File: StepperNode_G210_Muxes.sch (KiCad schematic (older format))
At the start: 6 parts

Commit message: Updated node core connector pages and added interlocks.
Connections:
- net labels removed: CHA_STEP_DIR
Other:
- note added: "Direction High = B-Y"
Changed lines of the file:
@@
 	7150 3700 7950 3700
-Wire Wire Line
-	7150 3800 7950 3800
 Wire Wire Line
 	7150 3900 7950 3900
@@
 	0    1    1    0
 $EndComp
-Text Label 7200 3500 0    60   ~ 0
-CHA_STEP2_STEP
-Text Label 7200 3600 0    60   ~ 0
-CHB_STEP2_STEP
 Text Label 7200 3700 0    60   ~ 0
 STEP2_STEP
-Text Label 7200 3800 0    60   ~ 0
-CHA_STEP2_DIR
-Text Label 7200 3900 0    60   ~ 0
-CHB_STEP2_DIR
 Text Label 7200 4000 0    60   ~ 0
 STEP2_DIR
-Text Label 5350 3500 0    60   ~ 0
-CHB_STEP1_DIR
 Text Label 5350 3600 0    60   ~ 0
 STEP1_DIR
-Text Label 5350 3700 0    60   ~ 0
-CHA_STEP1_STEP
-Text Label 5350 3800 0    60   ~ 0
-CHB_STEP1_STEP
 Text Label 5350 3900 0    60   ~ 0
 STEP1_STEP
@@
 	0    1    1    0
 $EndComp
-Text Label 7200 5300 0    60   ~ 0
-CHA_STEP4_STEP
-Text Label 7200 5400 0    60   ~ 0
-CHB_STEP4_STEP
-Text Label 7200 5500 0    60   ~ 0
-STEP4_STEP
-Text Label 7200 5600 0    60   ~ 0
-CHA_STEP4_DIR
-Text Label 7200 5700 0    60   ~ 0
-CHB_STEP4_DIR
 Text Label 7200 5800 0    60   ~ 0
 STEP4_DIR
-Text Label 5350 5200 0    60   ~ 0
-CHA_STEP3_DIR
-Text Label 5350 5300 0    60   ~ 0
-CHB_STEP3_DIR
 Text Label 5350 5400 0    60   ~ 0
 STEP3_DIR
-Text Label 5350 5500 0    60   ~ 0
-CHA_STEP3_STEP
-Text Label 5350 5600 0    60   ~ 0
-CHB_STEP3_STEP
 Text Label 5350 5700 0    60   ~ 0
 STEP3_STEP
@@
 	0    1    1    0
 $EndComp
-Text Label 7000 7550 0    60   ~ 0
-CHA_STEP6_STEP
-Text Label 7000 7650 0    60   ~ 0
-CHB_STEP6_STEP
 Text Label 7000 7750 0    60   ~ 0
 STEP6_STEP
-Text Label 7000 7850 0    60   ~ 0
-CHA_STEP6_DIR
-Text Label 7000 7950 0    60   ~ 0
-CHB_STEP6_DIR
 Text Label 7000 8050 0    60   ~ 0
 STEP6_DIR
-Text Label 5150 7450 0    60   ~ 0
-CHA_STEP5_DIR
-Text Label 5150 7550 0    60   ~ 0
-CHB_STEP5_DIR
 Text Label 5150 7650 0    60   ~ 0
 STEP5_DIR
-Text Label 5150 7750 0    60   ~ 0
-CHA_STEP5_STEP
-Text Label 5150 7850 0    60   ~ 0
-CHB_STEP5_STEP
 Text Label 5150 7950 0    60   ~ 0
 STEP5_STEP
@@
 Text HLabel 5150 3300 0    60   Input ~ 0
 STEP_DIR_CTRL
+Text HLabel 5150 3500 0    60   Input ~ 0
+CHA_STEP1_DIR
+Text HLabel 5150 3800 0    60   Input ~ 0
+CHA_STEP1_STEP
+Text HLabel 7950 3800 2    60   Input ~ 0
+CHB_STEP2_DIR
+Text HLabel 7950 3600 2    60   Input ~ 0
+CHA_STEP2_STEP
 Text HLabel 5150 3400 0    60   Input ~ 0
-CHA_STEP1_DIR
+CHB_STEP1_DIR
 Text HLabel 5150 3700 0    60   Input ~ 0
-CHA_STEP1_STEP
+CHB_STEP1_STEP
 Text HLabel 7950 3900 2    60   Input ~ 0
-CHB_STEP2_DIR
+CHA_STEP2_DIR
 Text HLabel 7950 3500 2    60   Input ~ 0
-CHA_STEP2_STEP
-Text Label 5350 3400 0    60   ~ 0
-CHA_STEP_DIR
-Text HLabel 5150 3500 0    60   Input ~ 0
-CHB_STEP1_DIR
-Text HLabel 5150 3800 0    60   Input ~ 0
-CHB_STEP1_STEP
-Text HLabel 7950 3800 2    60   Input ~ 0
-CHA_STEP2_DIR
-Text HLabel 7950 3600 2    60   Input ~ 0
 CHB_STEP2_STEP
+Text HLabel 5150 5300 0    60   Input ~ 0
+CHA_STEP3_DIR
+Text HLabel 5150 5600 0    60   Input ~ 0
+CHA_STEP3_STEP
 Text HLabel 5150 5200 0    60   Input ~ 0
-CHA_STEP3_DIR
+CHB_STEP3_DIR
 Text HLabel 5150 5500 0    60   Input ~ 0
-CHA_STEP3_STEP
-Text HLabel 5150 5300 0    60   Input ~ 0
-CHB_STEP3_DIR
-Text HLabel 5150 5600 0    60   Input ~ 0
 CHB_STEP3_STEP
+Text HLabel 7950 5600 2    60   Input ~ 0
+CHB_STEP4_DIR
+Text HLabel 7950 5400 2    60   Input ~ 0
+CHA_STEP4_STEP
 Text HLabel 7950 5700 2    60   Input ~ 0
-CHB_STEP4_DIR
+CHA_STEP4_DIR
 Text HLabel 7950 5300 2    60   Input ~ 0
-CHA_STEP4_STEP
-Text HLabel 7950 5600 2    60   Input ~ 0
-CHA_STEP4_DIR
-Text HLabel 7950 5400 2    60   Input ~ 0
 CHB_STEP4_STEP
+Text HLabel 4950 7550 0    60   Input ~ 0
+CHA_STEP5_DIR
+Text HLabel 4950 7850 0    60   Input ~ 0
+CHA_STEP5_STEP
 Text HLabel 4950 7450 0    60   Input ~ 0
-CHA_STEP5_DIR
+CHB_STEP5_DIR
 Text HLabel 4950 7750 0    60   Input ~ 0
-CHA_STEP5_STEP
-Text HLabel 4950 7550 0    60   Input ~ 0
-CHB_STEP5_DIR
-Text HLabel 4950 7850 0    60   Input ~ 0
 CHB_STEP5_STEP
+Text HLabel 7750 7850 2    60   Input ~ 0
+CHB_STEP6_DIR
+Text HLabel 7750 7650 2    60   Input ~ 0
+CHA_STEP6_STEP
 Text HLabel 7750 7950 2    60   Input ~ 0
-CHB_STEP6_DIR
+CHA_STEP6_DIR
 Text HLabel 7750 7550 2    60   Input ~ 0
-CHA_STEP6_STEP
-Text HLabel 7750 7850 2    60   Input ~ 0
-CHA_STEP6_DIR
-Text HLabel 7750 7650 2    60   Input ~ 0
 CHB_STEP6_STEP
+Text Notes 4350 2650 0    60   ~ 0
+Direction High = B-Y
+Wire Wire Line
+	7150 3800 7950 3800
+Text Label 7200 5500 0    60   ~ 0
+STEP4_STEP
 $EndSCHEMATC

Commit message: Remove Gimbal Functions
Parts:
- removed P? (x2): CONN_01X08_2MNT, symbol CONN_01X08_2MNT
- removed U? (x3): 74HCT157, symbol 74HCT157
- added C?: C_100nF_50V, RLOOP_FOOTPRINTS:rLoop_C_0603, symbol C_100nF_50V
- added U?: SN74HCT157D, RLOOP_FOOTPRINTS:rLoop_SOIC_16, symbol SN74HCT157D
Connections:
- net labels added: BRAKE1_DIR, BRAKE1_STEP, BRAKE2_DIR, BRAKE2_STEP, CHA_BRAKE1_DIR, CHA_BRAKE1_STEP, CHA_BRAKE2_DIR, CHA_BRAKE2_STEP, CHB_BRAKE1_DIR, CHB_BRAKE1_STEP, CHB_BRAKE2_DIR, CHB_BRAKE2_STEP
- net labels removed: CHA_STEP1_DIR, CHA_STEP1_STEP, CHA_STEP2_DIR, CHA_STEP2_STEP, CHA_STEP3_DIR, CHA_STEP3_STEP, CHA_STEP4_DIR, CHA_STEP4_STEP, CHA_STEP5_DIR, CHA_STEP5_STEP, CHA_STEP6_DIR, CHA_STEP6_STEP, CHB_STEP1_DIR, CHB_STEP1_STEP, CHB_STEP2_DIR, CHB_STEP2_STEP, CHB_STEP3_DIR, CHB_STEP3_STEP, CHB_STEP4_DIR, CHB_STEP4_STEP, CHB_STEP5_DIR, CHB_STEP5_STEP, CHB_STEP6_DIR, CHB_STEP6_STEP, STEP1_DIR, STEP1_STEP, STEP2_DIR, STEP2_STEP, STEP3_DIR, STEP3_STEP, STEP4_DIR, STEP4_STEP, STEP5_DIR, STEP5_STEP, STEP6_DIR, STEP6_STEP
- wire segments 60 -> 20
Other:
- note added: "Left and Right Brake Controllers"
- note removed: "15TTL load output capacity"
- note removed: "Fwd Left and Aft Left Gimbal Controller"
- note removed: "Fwd Right and Aft Right Gimbal Controller"
- note removed: "Left and Right brake controller."
- note removed: "Step 1 and 2, Left and Right brake drive controllers."
- note removed: "Step 3 and 4, Fwd Left and Aft Left Gimbal"
- note removed: "Step 5 and 6, Fwd Right and Aft Right Gimbal"

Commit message: First Revision -
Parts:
- removed P?: CONN_01X08_2MNT, symbol CONN_01X08_2MNT
- added P1: TE_640456-8, RLOOP_FOOTPRINTS:rLoop_TE640456-8, symbol TE_640456-8
- gave numbers to parts that had none: 2
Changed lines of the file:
@@
 Text Notes 5000 3500 0    60   ~ 0
 At 5V, VinH = 2V\nSafe to interface with 3.3V
-$Comp
-L CONN_01X08_2MNT P?
-U 1 1 575000E8
-P 12700 4300
-F 0 "P?" H 12700 4750 50  0000 C CNN
-F 1 "CONN_01X08_2MNT" V 12800 4300 50  0000 C CNN
-F 2 "" H 12700 4300 50  0000 C CNN
-F 3 "" H 12700 4300 50  0000 C CNN
-	1    12700 4300
-	1    0    0    -1
-$EndComp
 Text Notes 12150 4950 0    60   ~ 0
 Left and Right Brake Controllers
@@
 	12500 4350 11650 4350
 $Comp
-L GNDD #PWR?
+L GNDD #PWR6
 U 1 1 575000F3
 P 12500 4150
-F 0 "#PWR?" H 12500 3900 50  0001 C CNN
+F 0 "#PWR6" H 12500 3900 50  0001 C CNN
 F 1 "GNDD" H 12500 4000 50  0000 C CNN
 F 2 "" H 12500 4150 50  0000 C CNN
@@
 $EndComp
 $Comp
-L GNDD #PWR?
+L GNDD #PWR7
 U 1 1 575000F9
 P 12500 4450
-F 0 "#PWR?" H 12500 4200 50  0001 C CNN
+F 0 "#PWR7" H 12500 4200 50  0001 C CNN
 F 1 "GNDD" H 12500 4300 50  0000 C CNN
 F 2 "" H 12500 4450 50  0000 C CNN
@@
 Text Label 11750 4350 0    60   ~ 0
 BRAKE2_STEP
-Text Notes 13100 4700 1    60   ~ 0
+Text Notes 13900 4650 1    60   ~ 0
 Twisted pair wiring\nGrounded at this end only
 Text Notes 12000 10500 0    60   ~ 0
@@
 	6250 4350 5350 4350
 $Comp
-L GNDD #PWR?
+L GNDD #PWR4
 U 1 1 57503774
 P 7400 3850
-F 0 "#PWR?" H 7400 3600 50  0001 C CNN
+F 0 "#PWR4" H 7400 3600 50  0001 C CNN
 F 1 "GNDD" H 7400 3700 50  0000 C CNN
 F 2 "" H 7400 3850 50  0000 C CNN
@@
 	7350 3850 7400 3850
 $Comp
-L GNDD #PWR?
+L GNDD #PWR3
 U 1 1 5750377B
 P 6250 4450
-F 0 "#PWR?" H 6250 4200 50  0001 C CNN
+F 0 "#PWR3" H 6250 4200 50  0001 C CNN
 F 1 "GNDD" H 6250 4300 50  0000 C CNN
 F 2 "" H 6250 4450 50  0000 C CNN
@@
 STEP_DIR_CTRL
 $Comp
-L +5V #PWR?
+L +5V #PWR5
 U 1 1 5750378E
 P 7450 3550
-F 0 "#PWR?" H 7450 3400 50  0001 C CNN
+F 0 "#PWR5" H 7450 3400 50  0001 C CNN
 F 1 "+5V" H 7450 3690 50  0000 C CNN
 F 2 "" H 7450 3550 50  0000 C CNN
@@
 Direction High = B-Y
 $Comp
-L SN74HCT157D U?
+L SN74HCT157D U1
 U 1 1 57593B9D
 P 6450 4500
-F 0 "U?" H 7100 4450 59  0000 C CNN
+F 0 "U1" H 7100 4450 59  0000 C CNN
 F 1 "SN74HCT157D" H 6900 5400 59  0000 C CNN
 F 2 "RLOOP_FOOTPRINTS:rLoop_SOIC_16" H 7000 4350 197 0001 C CNN
@@
 $EndComp
 $Comp
-L C_100nF_50V C?
+L C_100nF_50V C1
 U 1 1 57593BE4
 P 5250 5250
-F 0 "C?" H 5275 5350 50  0000 L CNN
+F 0 "C1" H 5275 5350 50  0000 L CNN
 F 1 "C_100nF_50V" H 5275 5150 50  0000 L CNN
 F 2 "RLOOP_FOOTPRINTS:rLoop_C_0603" H 5288 5100 50  0001 C CNN
@@
 $EndComp
 $Comp
-L GNDD #PWR?
+L GNDD #PWR2
 U 1 1 57593C34
 P 5250 5400
-F 0 "#PWR?" H 5250 5150 50  0001 C CNN
+F 0 "#PWR2" H 5250 5150 50  0001 C CNN
 F 1 "GNDD" H 5250 5250 50  0000 C CNN
 F 2 "" H 5250 5400 50  0000 C CNN
@@
 $EndComp
 $Comp
-L +5V #PWR?
+L +5V #PWR1
 U 1 1 57593CAA
 P 5250 5100
-F 0 "#PWR?" H 5250 4950 50  0001 C CNN
+F 0 "#PWR1" H 5250 4950 50  0001 C CNN
 F 1 "+5V" H 5250 5240 50  0000 C CNN
 F 2 "" H 5250 5100 50  0000 C CNN
@@
 Text HLabel 5350 3750 0    60   Input ~ 0
 STEP_DIR_CTRL
+$Comp
+L TE_640456-8 P1
+U 1 1 5765ED3F
+P 12650 3900
+F 0 "P1" H 12700 3950 50  0000 C CNN
+F 1 "TE_640456-8" V 12800 3500 50  0000 C CNN
+F 2 "RLOOP_FOOTPRINTS:rLoop_TE640456-8" H 12700 3500 50  0001 C CNN
+F 3 "" H 12700 3500 50  0000 C CNN
+	1    12650 3900
+	1    0    0    -1
+$EndComp
 $EndSCHEMATC

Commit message: Update per design review.
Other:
- note removed: "The purpose of this block is to route 6 Step and 6 Direction signals from each of the two teensys and also buffer those signals.\n"
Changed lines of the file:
@@
 Text Notes 11950 10350 0    118  ~ 0
 rLoop - Stepper Node\nG210x Multiplexer Interface
-Text Notes 600  650  0    60   ~ 0
-The purpose of this block is to route 6 Step and 6 Direction signals from each of the two teensys and also buffer those signals.\n
 Text Notes 5000 3500 0    60   ~ 0
 At 5V, VinH = 2V\nSafe to interface with 3.3V

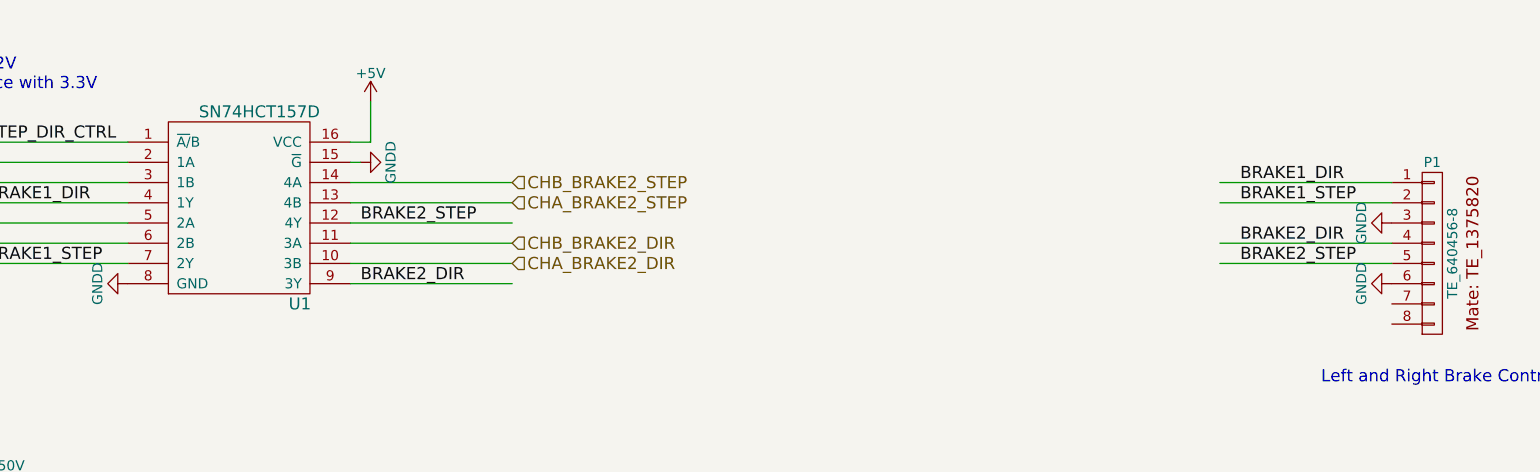
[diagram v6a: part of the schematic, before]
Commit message: Fix most ERC warnings (non-connected pins, etc)
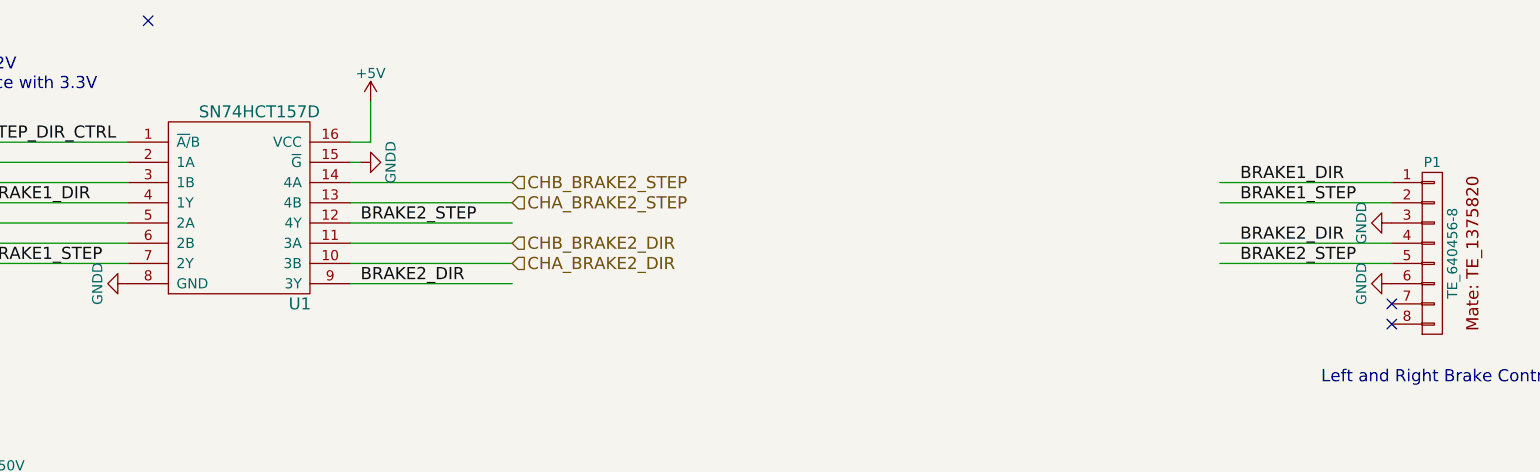
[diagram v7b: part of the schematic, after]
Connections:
- no-connect marks 0 -> 3
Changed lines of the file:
@@
 	12500 4350 11650 4350
 $Comp
-L GNDD #PWR6
+L GNDD #PWR01
 U 1 1 575000F3
 P 12500 4150
-F 0 "#PWR6" H 12500 3900 50  0001 C CNN
+F 0 "#PWR01" H 12500 3900 50  0001 C CNN
 F 1 "GNDD" H 12500 4000 50  0000 C CNN
 F 2 "" H 12500 4150 50  0000 C CNN
@@
 $EndComp
 $Comp
-L GNDD #PWR7
+L GNDD #PWR02
 U 1 1 575000F9
 P 12500 4450
-F 0 "#PWR7" H 12500 4200 50  0001 C CNN
+F 0 "#PWR02" H 12500 4200 50  0001 C CNN
 F 1 "GNDD" H 12500 4300 50  0000 C CNN
 F 2 "" H 12500 4450 50  0000 C CNN
@@
 	6250 4350 5350 4350
 $Comp
-L GNDD #PWR4
+L GNDD #PWR03
 U 1 1 57503774
 P 7400 3850
-F 0 "#PWR4" H 7400 3600 50  0001 C CNN
+F 0 "#PWR03" H 7400 3600 50  0001 C CNN
 F 1 "GNDD" H 7400 3700 50  0000 C CNN
 F 2 "" H 7400 3850 50  0000 C CNN
@@
 	7350 3850 7400 3850
 $Comp
-L GNDD #PWR3
+L GNDD #PWR04
 U 1 1 5750377B
 P 6250 4450
-F 0 "#PWR3" H 6250 4200 50  0001 C CNN
+F 0 "#PWR04" H 6250 4200 50  0001 C CNN
 F 1 "GNDD" H 6250 4300 50  0000 C CNN
 F 2 "" H 6250 4450 50  0000 C CNN
@@
 STEP_DIR_CTRL
 $Comp
-L +5V #PWR5
+L +5V #PWR05
 U 1 1 5750378E
 P 7450 3550
-F 0 "#PWR5" H 7450 3400 50  0001 C CNN
+F 0 "#PWR05" H 7450 3400 50  0001 C CNN
 F 1 "+5V" H 7450 3690 50  0000 C CNN
 F 2 "" H 7450 3550 50  0000 C CNN
@@
 $EndComp
 $Comp
-L GNDD #PWR2
+L GNDD #PWR06
 U 1 1 57593C34
 P 5250 5400
-F 0 "#PWR2" H 5250 5150 50  0001 C CNN
+F 0 "#PWR06" H 5250 5150 50  0001 C CNN
 F 1 "GNDD" H 5250 5250 50  0000 C CNN
 F 2 "" H 5250 5400 50  0000 C CNN
@@
 $EndComp
 $Comp
-L +5V #PWR1
+L +5V #PWR07
 U 1 1 57593CAA
 P 5250 5100
-F 0 "#PWR1" H 5250 4950 50  0001 C CNN
+F 0 "#PWR07" H 5250 4950 50  0001 C CNN
 F 1 "+5V" H 5250 5240 50  0000 C CNN
 F 2 "" H 5250 5100 50  0000 C CNN
@@
 	1    0    0    -1
 $EndComp
+NoConn ~ 6350 3150
+NoConn ~ 12500 4550
+NoConn ~ 12500 4650
 $EndSCHEMATC

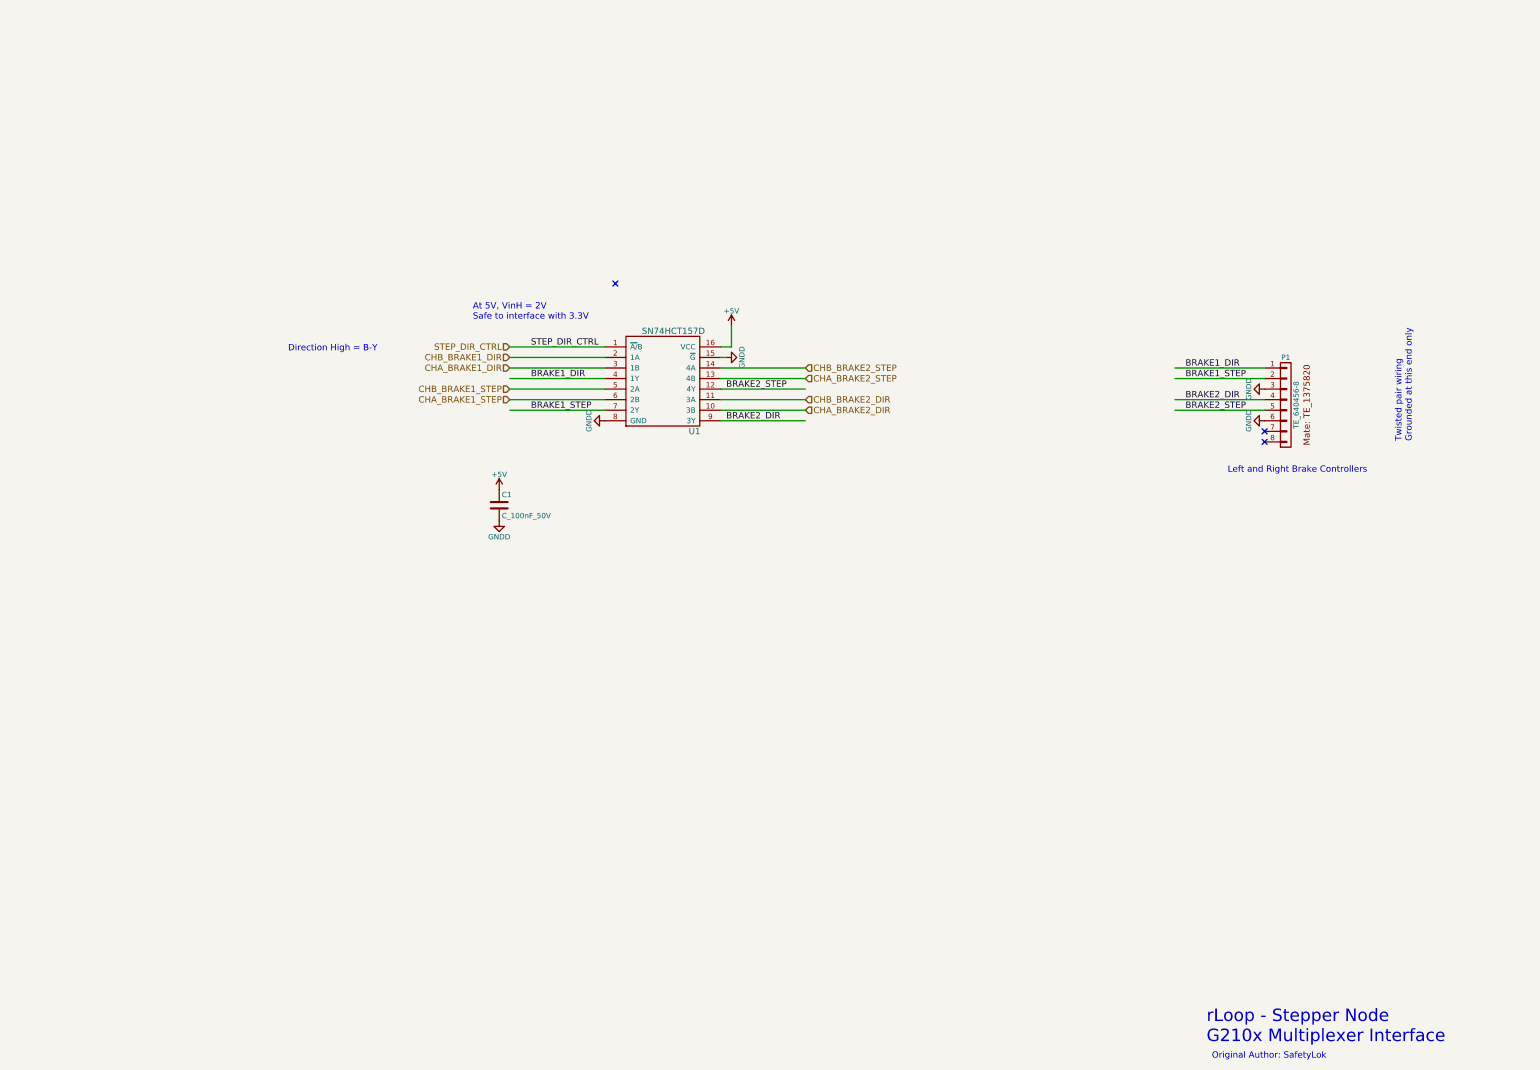
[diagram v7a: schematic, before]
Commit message: Finish isolation and add brake limit switches.
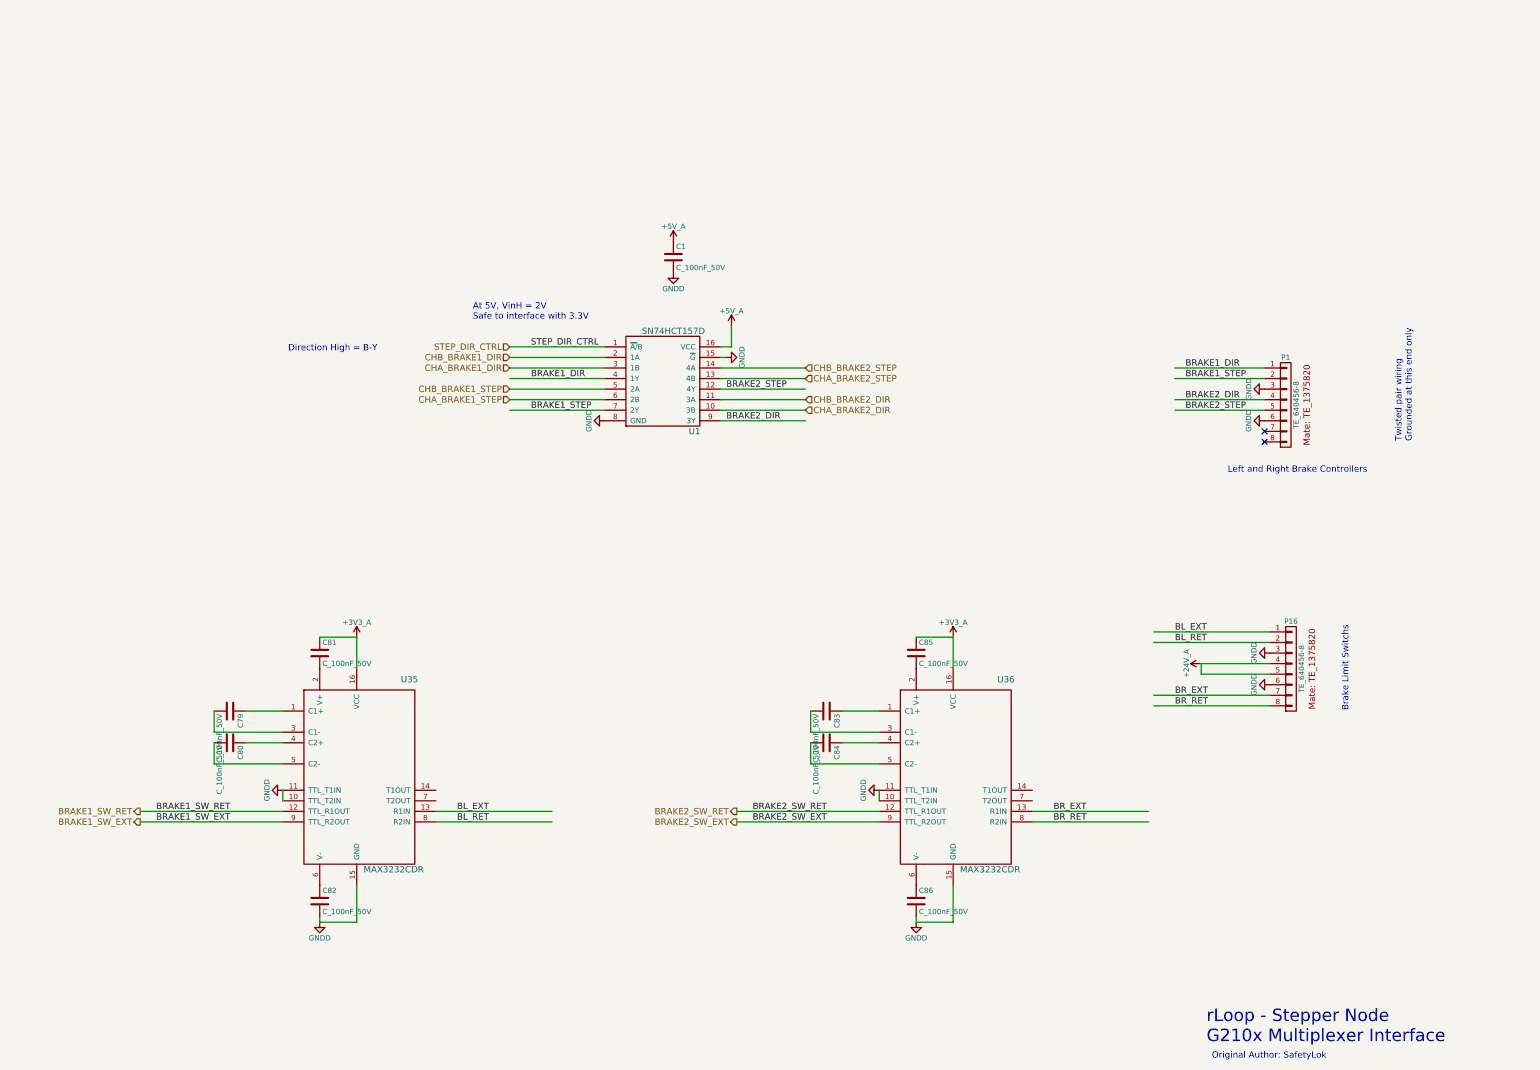
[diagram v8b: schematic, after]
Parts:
- added C79, C80, C81, C82, C83, C84, C85, C86: C_100nF_50V, RLOOP_FOOTPRINTS:rLoop_C_0603, symbol C_100nF_50V
- added P16: TE_640456-8, RLOOP_FOOTPRINTS:rLoop_TE640456-8, symbol TE_640456-8
- added U35, U36: MAX3232CDR, RLOOP_FOOTPRINTS:rLoop_SOIC_16, symbol MAX3232CDR
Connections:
- net labels added: +24V_A, +3V3_A, +5V_A, BL_EXT, BL_RET, BRAKE1_SW_EXT, BRAKE1_SW_RET, BRAKE2_SW_EXT, BRAKE2_SW_RET, BR_EXT, BR_RET
- net labels removed: +5V
- wire segments 20 -> 59
- no-connect marks 3 -> 2
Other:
- note added: "Brake Limit Switchs"
- moved on the sheet: C1
